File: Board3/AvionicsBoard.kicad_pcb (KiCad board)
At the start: 2 copper layers, 157.4 x 59 mm, 72 parts, among them J1 USB_A, J11 UART, J13 RFD900 Connector, J2 Conn_01x02, J6 Micro_SD_Card, U1 TL1963, U10 ECS-.327-12.5-17X-TR, U11 GT-U7_GPS, U12 LM340MP-5.0, U2 ATSAMD21G18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

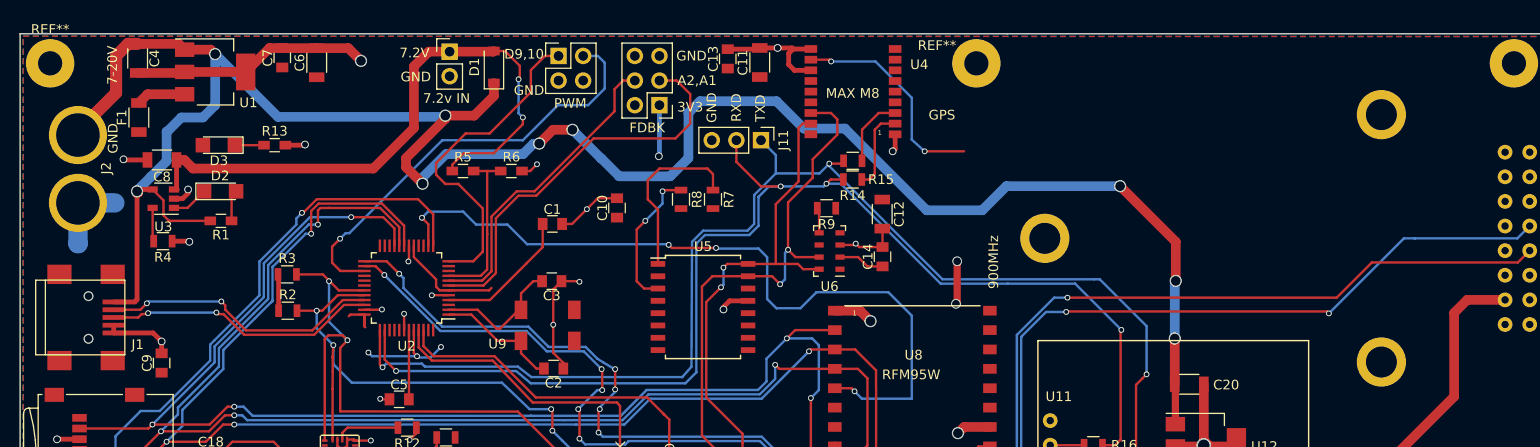
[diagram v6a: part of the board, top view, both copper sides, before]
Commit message: Add LEDs, cleanup traces
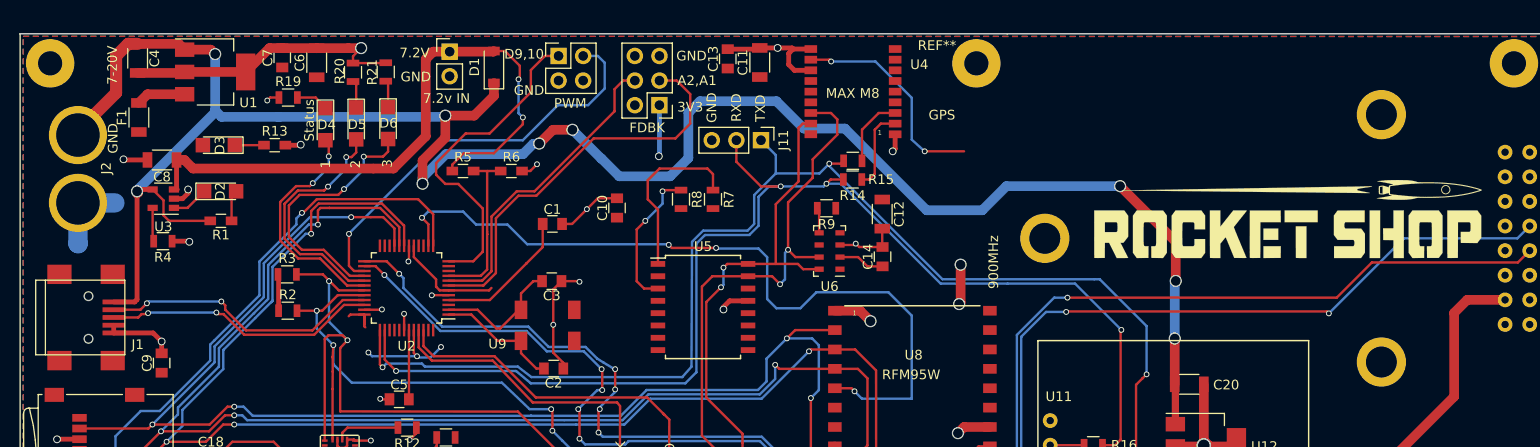
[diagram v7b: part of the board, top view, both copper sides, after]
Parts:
- added D4: LED, LEDs:LED_1206, F.Cu at (90.7, 60.1)
- added D5: LED, LEDs:LED_1206, F.Cu at (93.9, 60.0)
- added D6: LED, LEDs:LED_1206, F.Cu at (97.2, 60.0)
- added G***: LOGO, RocketShopLogos:RocketShopGraphicLogo, B.Cu at (105.8, 76.8)
- added G***: LOGO, RocketShopLogos:RocketShopGraphicLogo-Medium, F.Cu at (190.0, 69.9)
- added R19: 1K, Resistors_SMD:R_0805, F.Cu at (86.8, 57.4)
- added R20: 1K, Resistors_SMD:R_0805, F.Cu at (93.5, 54.8)
- added R21: 1K, Resistors_SMD:R_0805, F.Cu at (96.9, 54.7)
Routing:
- net /D12: track 0.00 -> 27.3 mm, vias 0 -> 2
- net /D6: track 0.00 -> 25.3 mm, vias 0 -> 2
- net /D7: track 0.00 -> 24.1 mm, vias 0 -> 2
- net VBUS: track 221.7 -> 217.0 mm
- net (no net): track 0.00 -> 4.23 mm, vias 0 -> 2
- net Net-(D4-Pad1): track 0.00 -> 3.39 mm
- net Net-(D5-Pad1): track 0.00 -> 2.81 mm
- net Net-(D6-Pad1): track 0.00 -> 2.77 mm
- net /D10: track 45.4 -> 42.9 mm
- net GND: track 156.4 -> 157.5 mm, vias 33 -> 32
- net +7.5V: track 64.5 -> 65.4 mm
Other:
- board text added: "1"
- board text added: "2"
- board text added: "3"
- board text added: "Avionics Board 3.1"
- board text added: "Status"
- board text removed: "Avionics Board"

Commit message: Added finshing touches to board. Investigate GPS and RFM95 RF paths!! RFD900 mounting hole sneed resizing!!
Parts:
- added G***: LOGO, RocketShopLogos:QRcode, F.Cu at (170.5, 58.0)
- added G***: LOGO, RocketShopLogos:shrug2, B.Cu at (111.8, 111.8)
- added J12: RF IN, FoxWestern:Edge_SMA, F.Cu at (213.6, 101.7)
- added J7: RF IN, FoxWestern:Edge_SMA, F.Cu at (213.6, 92.1)
- added REF***: ESD-Logo_13.2x12mm_SilkScreen, Symbols:ESD-Logo_13.2x12mm_SilkScreen, F.Cu at (186.2, 58.6)
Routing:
- net Net-(J7-Pad1): track 22.2 -> 95.3 mm
- net Net-(J12-Pad1): track 2.21 -> 67.7 mm, vias 1 -> 0
- net GND: track 157.5 -> 171.6 mm
- net (no net): track 4.23 -> 0.00 mm, vias 2 -> 0
- net +5V: track 52.9 -> 52.1 mm
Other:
- board text added: "RFM95"
